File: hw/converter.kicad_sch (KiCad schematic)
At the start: 7 parts

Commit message: working on documentation, design methmethodology, sizing, layout
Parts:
- removed J? (x2): Conn_01x02, Connector_PinHeader_2.54mm:PinHeader_1x02_P2.54mm_Horizontal, symbol Connector_Generic:Conn_01x02
- added C303, C304: 18uF, Capacitor_THT:CP_Radial_D10.0mm_P5.00mm, symbol Device:C
- added J301, J302: 1935776, 1935776, symbol 1935776:1935776
- C301: renamed from C?; value 10uF -> 5uF; footprint Capacitor_SMD:C_1210_3225Metric -> Capacitor_THT:CP_Axial_L10.0mm_D6.0mm_P15.00mm_Horizontal
- C302: renamed from C?; value 330uF -> 18uF; footprint Capacitor_THT:CP_Radial_D18.0mm_P7.50mm -> Capacitor_THT:CP_Radial_D10.0mm_P5.00mm
- Q301, Q302: renamed from Q?; footprint Package_TO_SOT_SMD:TO-263-2 -> mppt:EPC2307
- gave numbers to parts that had none: 1
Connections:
- net GND: now reaches C301.2, C302.2, Q301.3 (S)
- net GND: now also C303.2, C304.2
- net V_BATT+: now reaches C302.1, Q302.2 (D)
- net V_BATT+: now also C303.1, C304.1, J302.1
- net V_ARR+: now reaches C301.1, L301.1
- net V_ARR+: now also J301.1
- new net V_ARR-: J301.2
- new net V_BATT-: J302.2
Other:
- moved on the sheet: C301, C302, L301, Q301, Q302

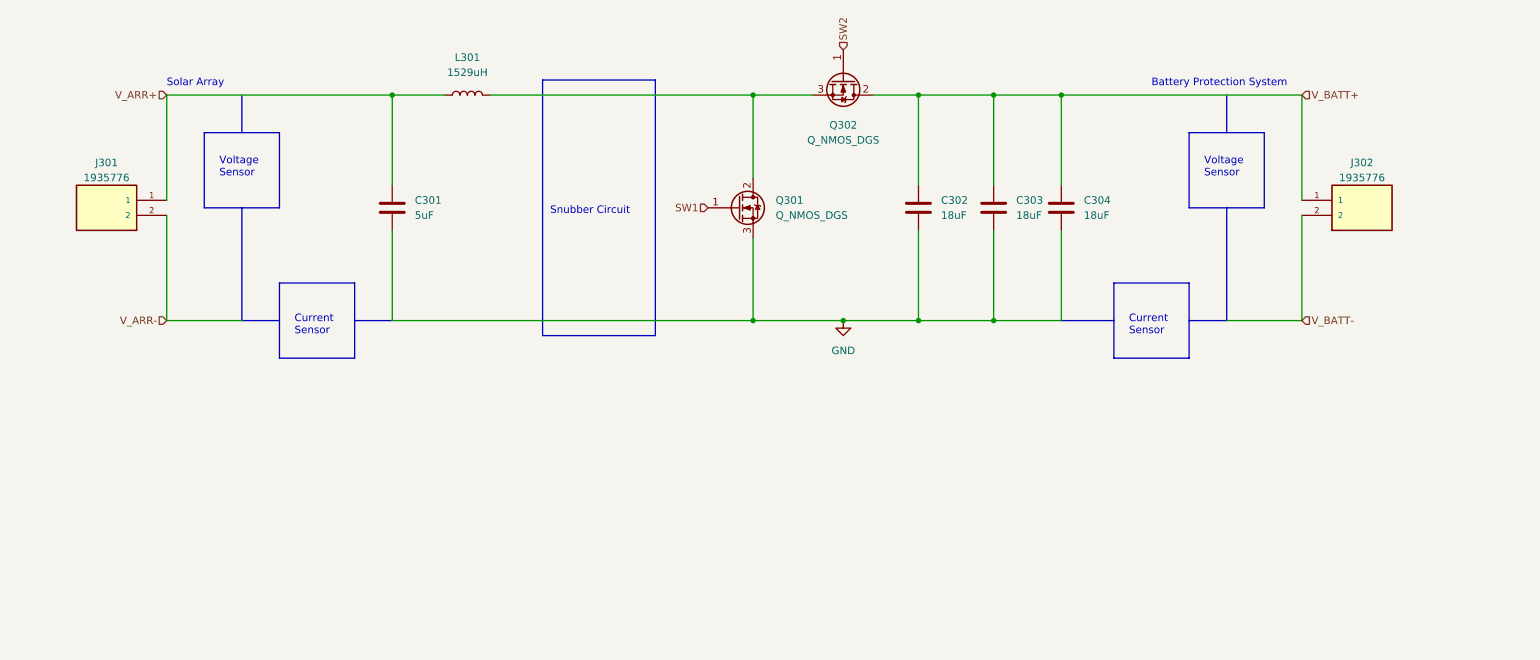
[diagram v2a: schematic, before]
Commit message: laid out MOSFET switching loop and thermal connections
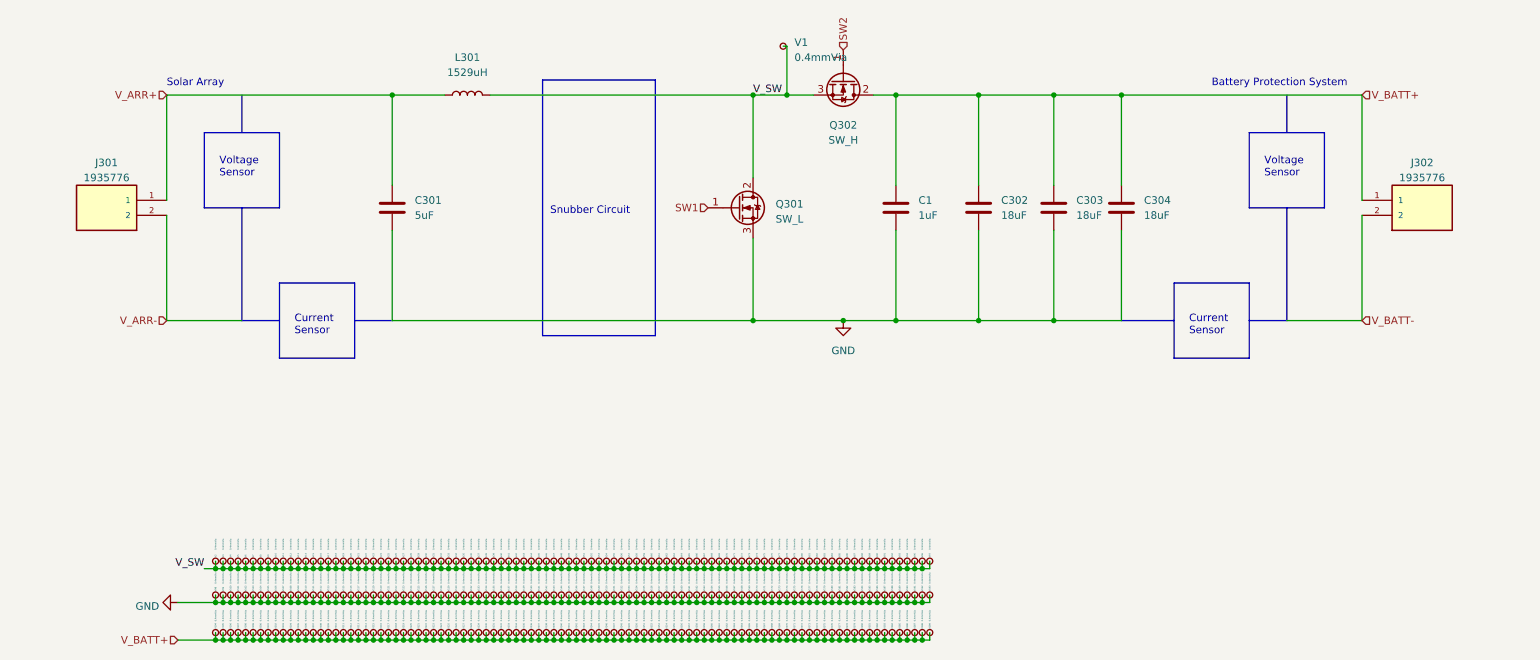
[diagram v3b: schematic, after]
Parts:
- added C1: 1uF, Capacitor_SMD:C_1812_4532Metric, symbol Device:C
- added V1, V10, V100, V101, V102, V103, V104, V105, V106, V107, V108, V109, V11, V110, V111, V112, V113, V114, V115, V116, V117, V118, V119, V12, V120, V121, V122, V123, V124, V125, V126, V127, V128, V129, V13, V130, V131, V132, V133, V134, V135, V136, V137, V138, V139, V14, V140, V141, V142, V143, V144, V145, V146, V147, V148, V149, V15, V150, V151, V152, V153, V154, V155, V156, V157, V158, V159, V16, V160, V161, V162, V163, V164, V165, V166, V167, V168, V169, V17, V170, V171, V172, V173, V174, V175, V176, V177, V178, V179, V18, V180, V181, V182, V183, V184, V185, V186, V187, V188, V189, V19, V190, V191, V192, V193, V194, V195, V196, V197, V198, V199, V2, V20, V200, V201, V202, V203, V204, V205, V206, V207, V208, V209, V21, V210, V211, V212, V213, V214, V215, V216, V217, V218, V219, V22, V220, V221, V222, V223, V224, V225, V226, V227, V228, V229, V23, V230, V231, V232, V233, V234, V235, V236, V237, V238, V239, V24, V240, V241, V242, V243, V244, V245, V246, V247, V248, V249, V25, V250, V251, V252, V253, V254, V255, V256, V257, V258, V259, V26, V260, V261, V262, V263, V264, V265, V266, V267, V268, V269, V27, V270, V271, V272, V273, V274, V275, V276, V277, V278, V279, V28, V280, V281, V282, V283, V284, V285, V286, V287, V288, V289, V29, V3, V30, V31, V32, V33, V34, V35, V36, V37, V38, V39, V4, V40, V41, V42, V43, V44, V45, V46, V47, V48, V49, V5, V50, V51, V52, V53, V54, V55, V56, V57, V58, V59, V6, V60, V61, V62, V63, V64, V65, V66, V67, V68, V69, V7, V70, V71, V72, V73, V74, V75, V76, V77, V78, V79, V8, V80, V81, V82, V83, V84, V85, V86, V87, V88, V89, V9, V90, V91, V92, V93, V94, V95, V96, V97, V98, V99: 0.4mmVia, mppt:Via_0.4mmOD_0.2mmID, symbol Connector:TestPoint_Small
- Q301: value Q_NMOS_DGS -> SW_L
- Q302: value Q_NMOS_DGS -> SW_H
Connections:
- net GND: now also C1.2, V100.1, V101.1, V102.1, V103.1, V104.1, V105.1, V106.1, V107.1, V108.1, V109.1, V110.1, V111.1, V112.1, V113.1, V114.1, V115.1, V116.1, V117.1, V118.1, V119.1, V120.1, V121.1, V122.1, V123.1, V124.1, V125.1, V126.1, V127.1, V128.1, V129.1, V130.1, V131.1, V132.1, V133.1, V134.1, V135.1, V136.1, V137.1, V138.1, V139.1, V140.1, V141.1, V142.1, V143.1, V144.1, V145.1, V146.1, V147.1, V148.1, V149.1, V150.1, V151.1, V152.1, V153.1, V154.1, V155.1, V156.1, V157.1, V158.1, V159.1, V160.1, V161.1, V162.1, V163.1, V164.1, V165.1, V166.1, V167.1, V168.1, V169.1, V170.1, V171.1, V172.1, V173.1, V174.1, V175.1, V176.1, V177.1, V178.1, V179.1, V180.1, V181.1, V182.1, V183.1, V184.1, V185.1, V186.1, V187.1, V188.1, V189.1, V190.1, V191.1, V192.1, V193.1, V98.1, V99.1
- net V_BATT+: now also C1.1, V194.1, V195.1, V196.1, V197.1, V198.1, V199.1, V200.1, V201.1, V202.1, V203.1, V204.1, V205.1, V206.1, V207.1, V208.1, V209.1, V210.1, V211.1, V212.1, V213.1, V214.1, V215.1, V216.1, V217.1, V218.1, V219.1, V220.1, V221.1, V222.1, V223.1, V224.1, V225.1, V226.1, V227.1, V228.1, V229.1, V230.1, V231.1, V232.1, V233.1, V234.1, V235.1, V236.1, V237.1, V238.1, V239.1, V240.1, V241.1, V242.1, V243.1, V244.1, V245.1, V246.1, V247.1, V248.1, V249.1, V250.1, V251.1, V252.1, V253.1, V254.1, V255.1, V256.1, V257.1, V258.1, V259.1, V260.1, V261.1, V262.1, V263.1, V264.1, V265.1, V266.1, V267.1, V268.1, V269.1, V270.1, V271.1, V272.1, V273.1, V274.1, V275.1, V276.1, V277.1, V278.1, V279.1, V280.1, V281.1, V282.1, V283.1, V284.1, V285.1, V286.1, V287.1, V288.1, V289.1
- net V_SW: now reaches L301.2, Q301.2 (D), Q302.3 (S)
- net V_SW: now also V1.1, V10.1, V11.1, V12.1, V13.1, V14.1, V15.1, V16.1, V17.1, V18.1, V19.1, V2.1, V20.1, V21.1, V22.1, V23.1, V24.1, V25.1, V26.1, V27.1, V28.1, V29.1, V3.1, V30.1, V31.1, V32.1, V33.1, V34.1, V35.1, V36.1, V37.1, V38.1, V39.1, V4.1, V40.1, V41.1, V42.1, V43.1, V44.1, V45.1, V46.1, V47.1, V48.1, V49.1, V5.1, V50.1, V51.1, V52.1, V53.1, V54.1, V55.1, V56.1, V57.1, V58.1, V59.1, V6.1, V60.1, V61.1, V62.1, V63.1, V64.1, V65.1, V66.1, V67.1, V68.1, V69.1, V7.1, V70.1, V71.1, V72.1, V73.1, V74.1, V75.1, V76.1, V77.1, V78.1, V79.1, V8.1, V80.1, V81.1, V82.1, V83.1, V84.1, V85.1, V86.1, V87.1, V88.1, V89.1, V9.1, V90.1, V91.1, V92.1, V93.1, V94.1, V95.1, V96.1, V97.1
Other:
- moved on the sheet: C302, C303, C304, J302

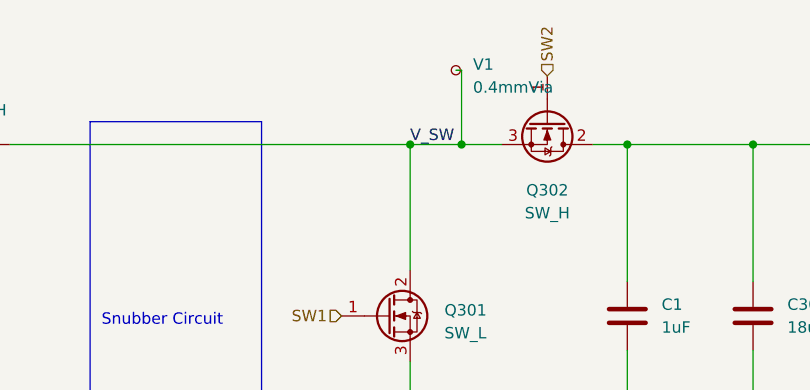
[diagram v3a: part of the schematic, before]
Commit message: made gate driver loop v1
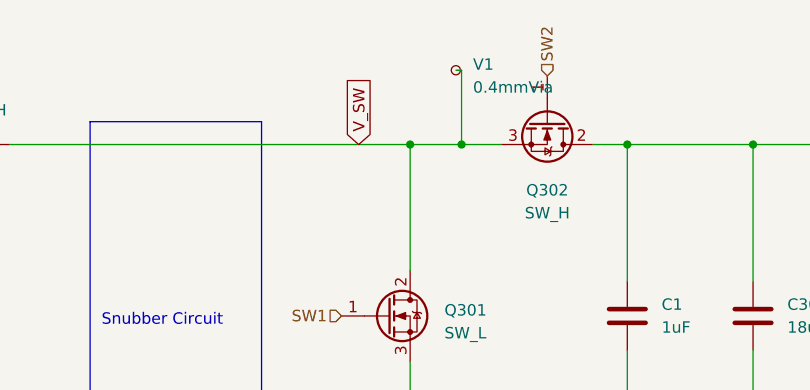
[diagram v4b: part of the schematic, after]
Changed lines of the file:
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@@
-    (effects (font (size 1.27 1.27)) (justify left bottom))
-  )
-  (label "V_SW" (at 151.13 68.58 0) (fields_autoplaced)
     (effects (font (size 1.27 1.27)) (justify left bottom))
   )
@@
     (effects (font (size 1.27 1.27)) (justify right bottom))
   )
+  (global_label "V_SW" (shape input) (at 145.415 68.58 90) (fields_autoplaced)
+    (effects (font (size 1.27 1.27)) (justify left))
+    (property "Intersheetrefs" "${INTERSHEET_REFS}" (at 145.415 60.9571 90)
+      (effects (font (size 1.27 1.27)) (justify left) hide)
+    )
+  )
   (hierarchical_label "V_ARR+" (shape input) (at 52.07 68.58 180) (fields_autoplaced)

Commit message: layout revision this one is cursed
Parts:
- removed V1, V10, V100, V101, V102, V103, V104, V105, V106, V107, V108, V109, V11, V110, V111, V112, V113, V114, V115, V116, V117, V118, V119, V12, V120, V121, V122, V123, V124, V125, V126, V127, V128, V129, V13, V130, V131, V132, V133, V134, V135, V136, V137, V138, V139, V14, V140, V141, V142, V143, V144, V145, V146, V147, V148, V149, V15, V150, V151, V152, V153, V154, V155, V156, V157, V158, V159, V16, V160, V161, V162, V163, V164, V165, V166, V167, V168, V169, V17, V170, V171, V172, V173, V174, V175, V176, V177, V178, V179, V18, V180, V181, V182, V183, V184, V185, V186, V187, V188, V189, V19, V190, V191, V192, V193, V194, V195, V196, V197, V198, V199, V2, V20, V200, V201, V202, V203, V204, V205, V206, V207, V208, V209, V21, V210, V211, V212, V213, V214, V215, V216, V217, V218, V219, V22, V220, V221, V222, V223, V224, V225, V226, V227, V228, V229, V23, V230, V231, V232, V233, V234, V235, V236, V237, V238, V239, V24, V240, V241, V242, V243, V244, V245, V246, V247, V248, V249, V25, V250, V251, V252, V253, V254, V255, V256, V257, V258, V259, V26, V260, V261, V262, V263, V264, V265, V266, V267, V268, V269, V27, V270, V271, V272, V273, V274, V275, V276, V277, V278, V279, V28, V280, V281, V282, V283, V284, V285, V286, V287, V288, V289, V29, V3, V30, V31, V32, V33, V34, V35, V36, V37, V38, V39, V4, V40, V41, V42, V43, V44, V45, V46, V47, V48, V49, V5, V50, V51, V52, V53, V54, V55, V56, V57, V58, V59, V6, V60, V61, V62, V63, V64, V65, V66, V67, V68, V69, V7, V70, V71, V72, V73, V74, V75, V76, V77, V78, V79, V8, V80, V81, V82, V83, V84, V85, V86, V87, V88, V89, V9, V90, V91, V92, V93, V94, V95, V96, V97, V98, V99: 0.4mmVia, mppt:Via_0.4mmOD_0.2mmID, symbol Connector:TestPoint_Small
- L301: value 1529uH -> 560; footprint Inductor_THT:L_CommonMode_Toroid_Vertical_L43.2mm_W22.9mm_Px17.78mm_Py30.48mm_Bourns_8100 -> mppt:B65812N1005D002

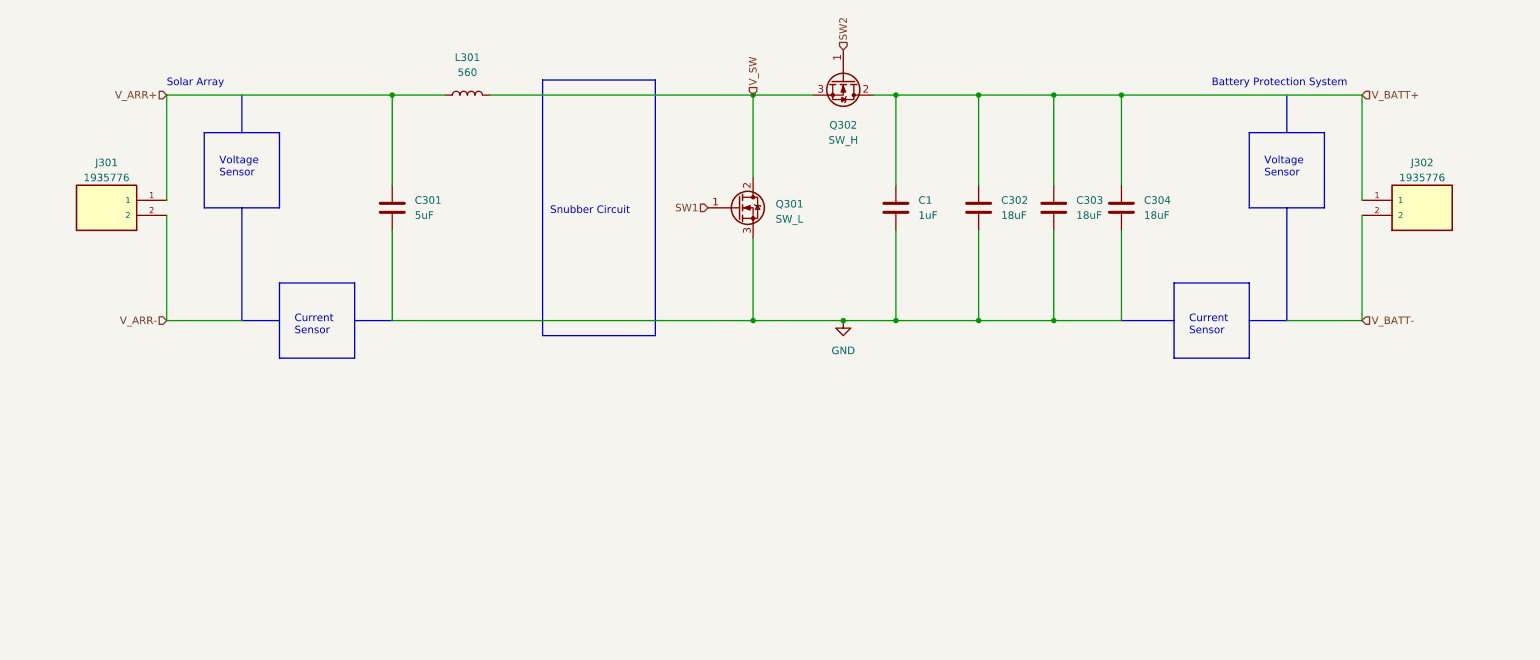
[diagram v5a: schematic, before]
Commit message: improved thermals of fets with internal vias, internal traces, and thermal jumpers
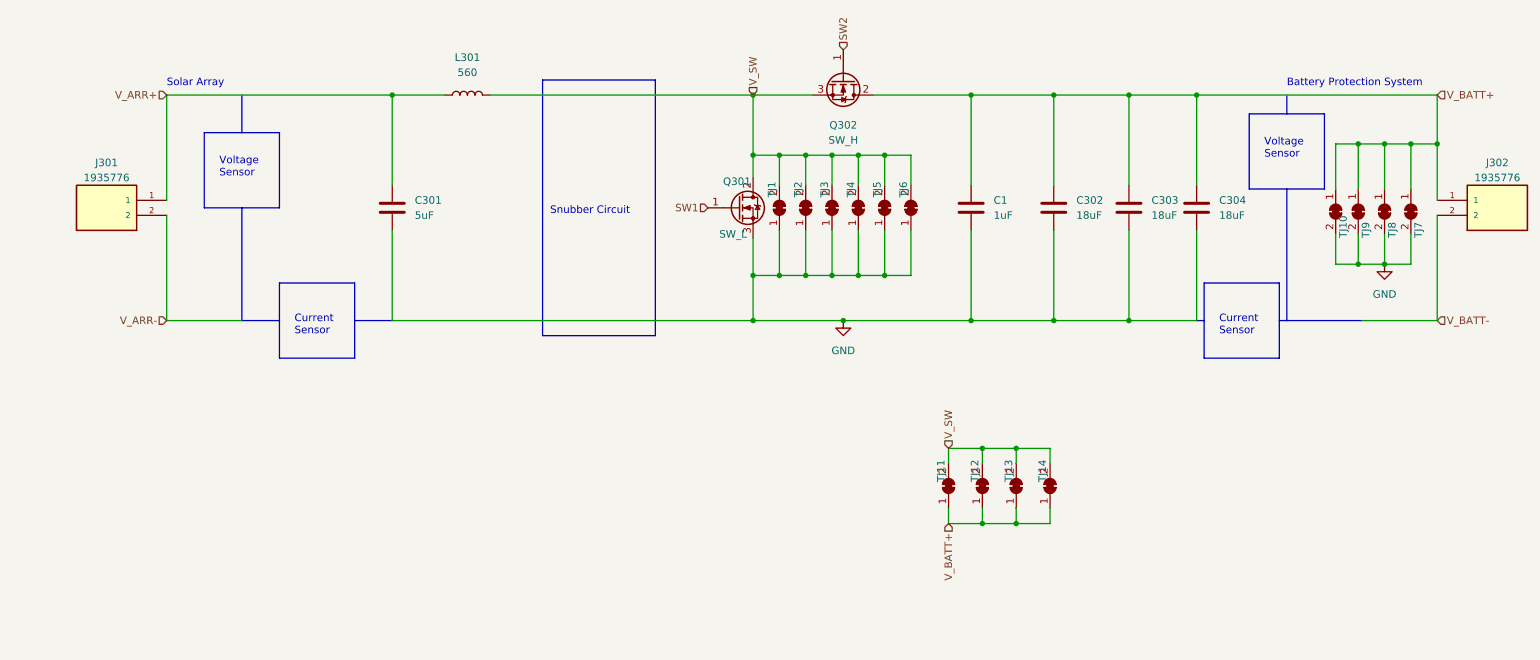
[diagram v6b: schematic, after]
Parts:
- added TJ1, TJ10, TJ11, TJ12, TJ13, TJ14, TJ2, TJ3, TJ4, TJ5, TJ6, TJ7, TJ8, TJ9: Thermal Jumper, Resistor_SMD:R_0603_1608Metric, symbol Jumper:SolderJumper_2_Bridged
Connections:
- net GND: now also TJ1.1 (A), TJ10.2 (B), TJ2.1 (A), TJ3.1 (A), TJ4.1 (A), TJ5.1 (A), TJ6.1 (A), TJ7.2 (B), TJ8.2 (B), TJ9.2 (B)
- net V_BATT+: now also TJ10.1 (A), TJ11.1 (A), TJ12.1 (A), TJ13.1 (A), TJ14.1 (A), TJ7.1 (A), TJ8.1 (A), TJ9.1 (A)
- net V_SW: now also TJ1.2 (B), TJ11.2 (B), TJ12.2 (B), TJ13.2 (B), TJ14.2 (B), TJ2.2 (B), TJ3.2 (B), TJ4.2 (B), TJ5.2 (B), TJ6.2 (B)
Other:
- moved on the sheet: C1, C302, C303, C304, J302

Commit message: even better thermal design, kept pours out of MOSFET pins and sswitched to 0805 thermal jumpers
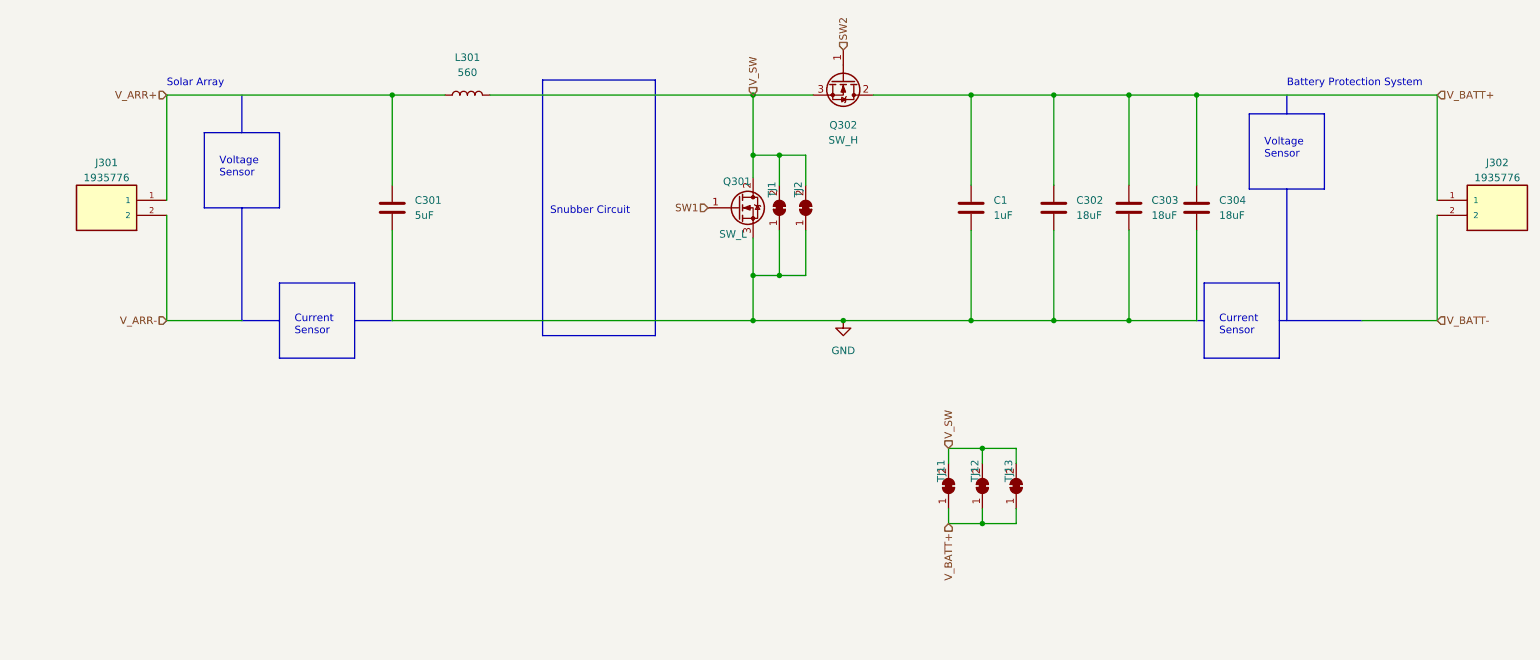
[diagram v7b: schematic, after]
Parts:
- removed TJ10, TJ14, TJ3, TJ4, TJ5, TJ6, TJ7, TJ8, TJ9: Thermal Jumper, Resistor_SMD:R_0603_1608Metric, symbol Jumper:SolderJumper_2_Bridged
- TJ1, TJ11, TJ12, TJ13, TJ2: footprint Resistor_SMD:R_0603_1608Metric -> Resistor_SMD:R_0805_2012Metric; Mfr PN (none) -> QB0805B40WYT

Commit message: revision of PCB layout
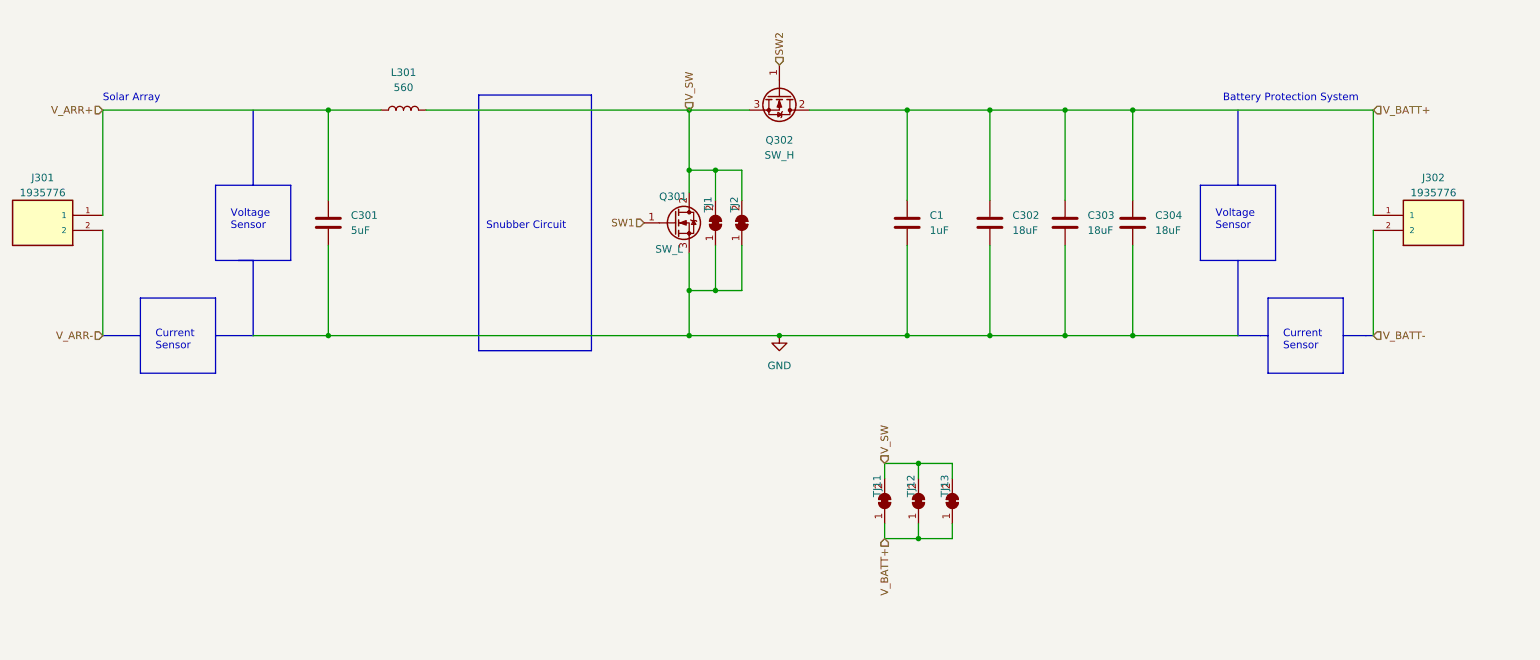
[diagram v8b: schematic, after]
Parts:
- C1: footprint Capacitor_SMD:C_1812_4532Metric -> Capacitor_SMD:C_2220_5650Metric
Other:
- moved on the sheet: C1, C301, C302, C303, C304, J301, J302, L301, Q301, Q302, TJ1, TJ11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
